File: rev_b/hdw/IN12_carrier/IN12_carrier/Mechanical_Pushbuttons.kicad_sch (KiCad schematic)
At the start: 1 part, among them U1101 MAX6818

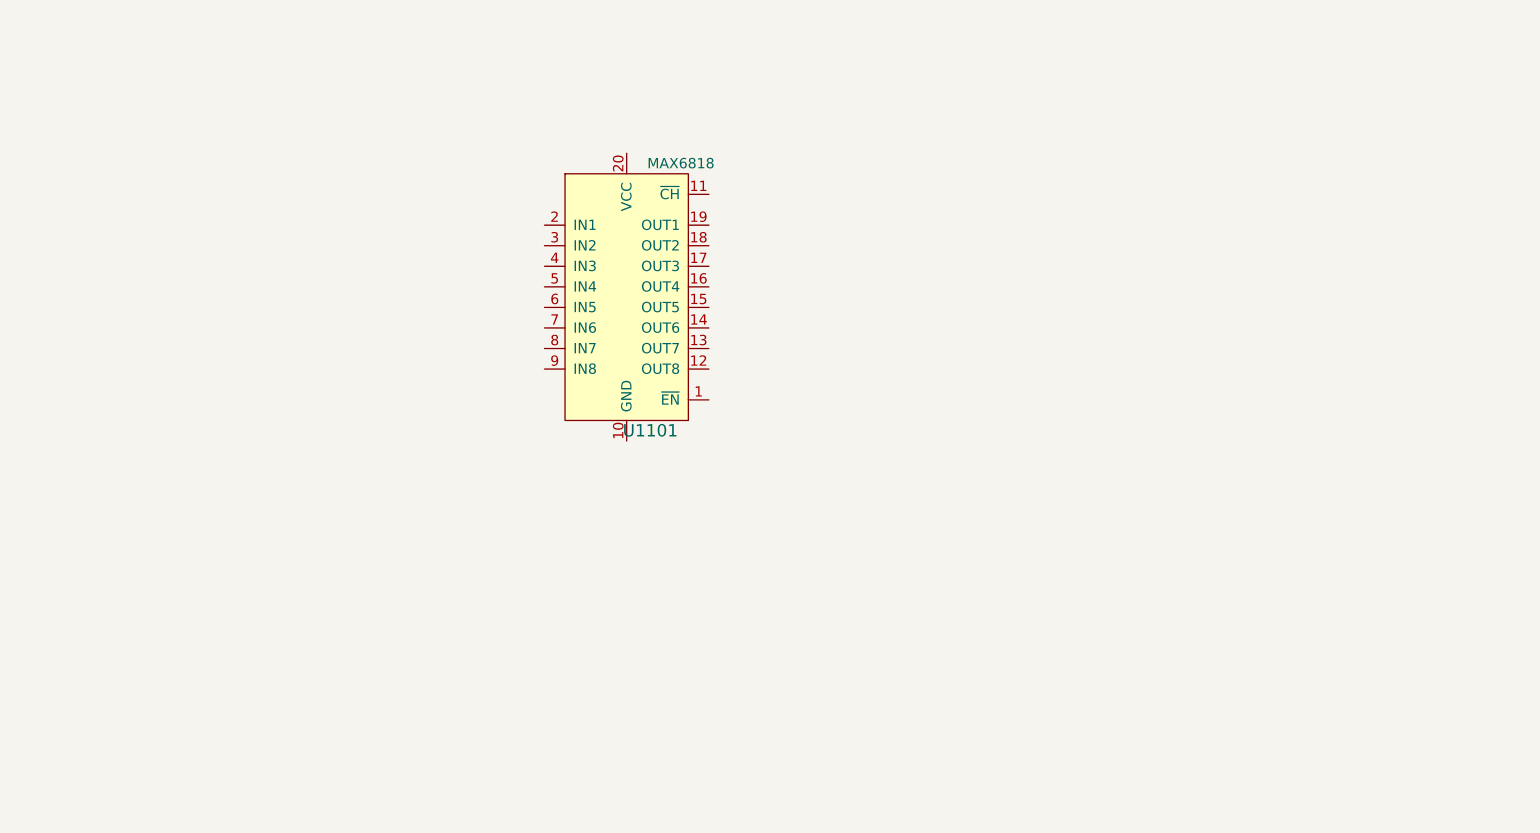
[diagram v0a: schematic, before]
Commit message: lots of placement progress on IN12 carrier board
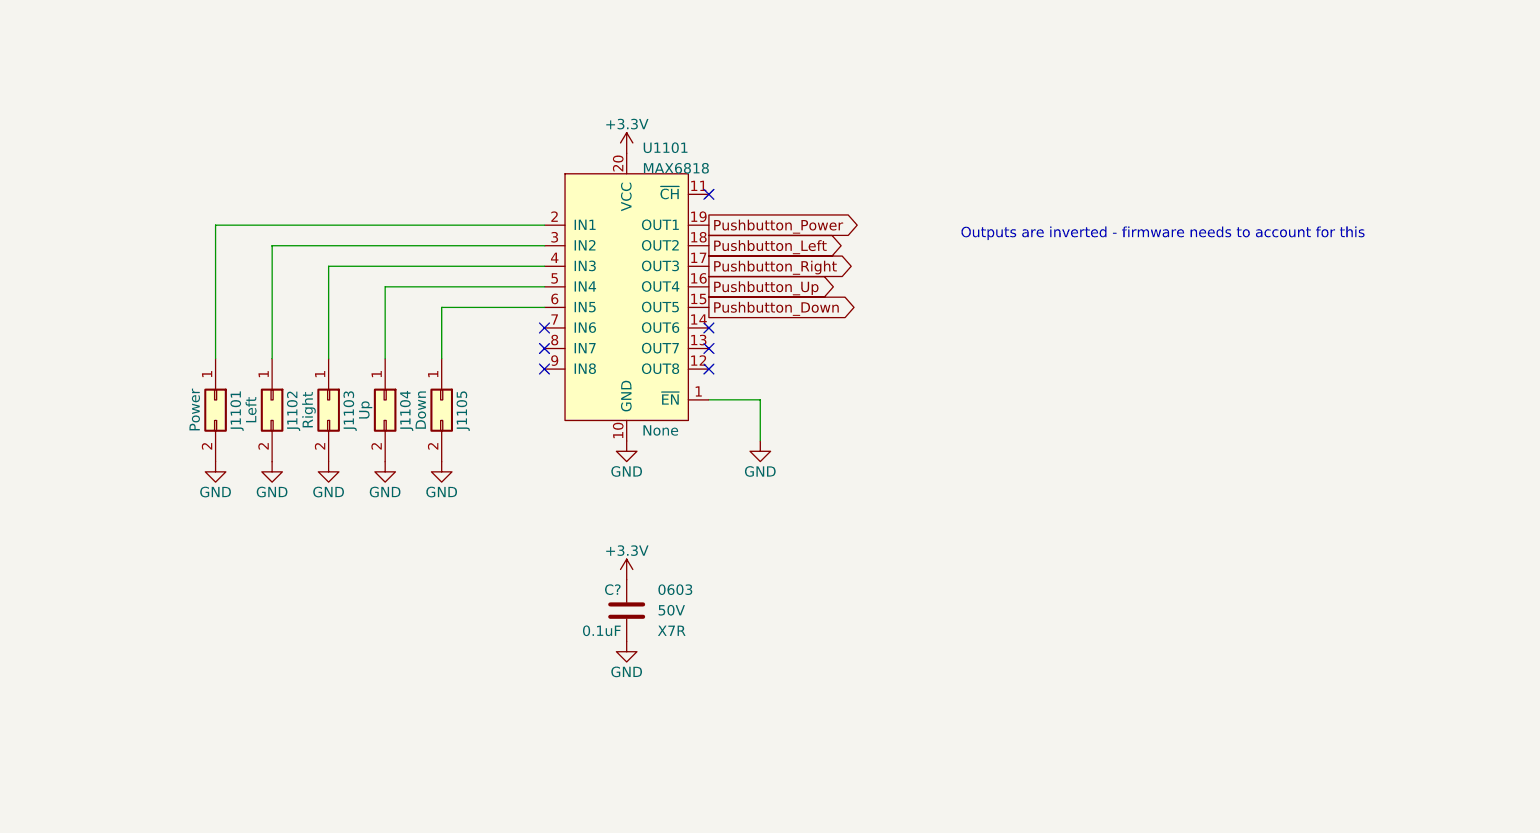
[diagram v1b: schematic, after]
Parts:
- added C?: 0.1uF, Capacitors_SMD:C_0603, symbol Custom_Library:C_Custom
- added J1101: Power, Connector_PinHeader_2.54mm:PinHeader_1x02_P2.54mm_Vertical, symbol Connector_Generic:Conn_02x01
- added J1102: Left, Connector_PinHeader_2.54mm:PinHeader_1x02_P2.54mm_Vertical, symbol Connector_Generic:Conn_02x01
- added J1103: Right, Connector_PinHeader_2.54mm:PinHeader_1x02_P2.54mm_Vertical, symbol Connector_Generic:Conn_02x01
- added J1104: Up, Connector_PinHeader_2.54mm:PinHeader_1x02_P2.54mm_Vertical, symbol Connector_Generic:Conn_02x01
- added J1105: Down, Connector_PinHeader_2.54mm:PinHeader_1x02_P2.54mm_Vertical, symbol Connector_Generic:Conn_02x01
- U1101: Configuration (none) -> None
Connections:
- net GND: now reaches U1101.1 (~{EN})
- net GND: now also U1101.10 (GND), C?.2, J1101.2 (Pin_2), J1102.2 (Pin_2), J1103.2 (Pin_2), J1104.2 (Pin_2), J1105.2 (Pin_2)
- net Pushbutton_Down: now reaches U1101.15 (OUT5)
- net Pushbutton_Up: now reaches U1101.16 (OUT4)
- net Pushbutton_Right: now reaches U1101.17 (OUT3)
- net Pushbutton_Left: now reaches U1101.18 (OUT2)
- net Pushbutton_Power: now reaches U1101.19 (OUT1)
- net at U1101.2 (IN1): now also J1101.1 (Pin_1)
- net +3.3V: now reaches U1101.20 (VCC)
- net +3.3V: now also C?.1
- net at U1101.3 (IN2): now also J1102.1 (Pin_1)
- net at U1101.4 (IN3): now also J1103.1 (Pin_1)
- net at U1101.5 (IN4): now also J1104.1 (Pin_1)
- net at U1101.6 (IN5): now also J1105.1 (Pin_1)
- no-connect marks 0 -> 7
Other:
- note added: "Outputs are inverted - firmware needs to account for this"

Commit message: lots of routing and design progress on IN12 carrier board
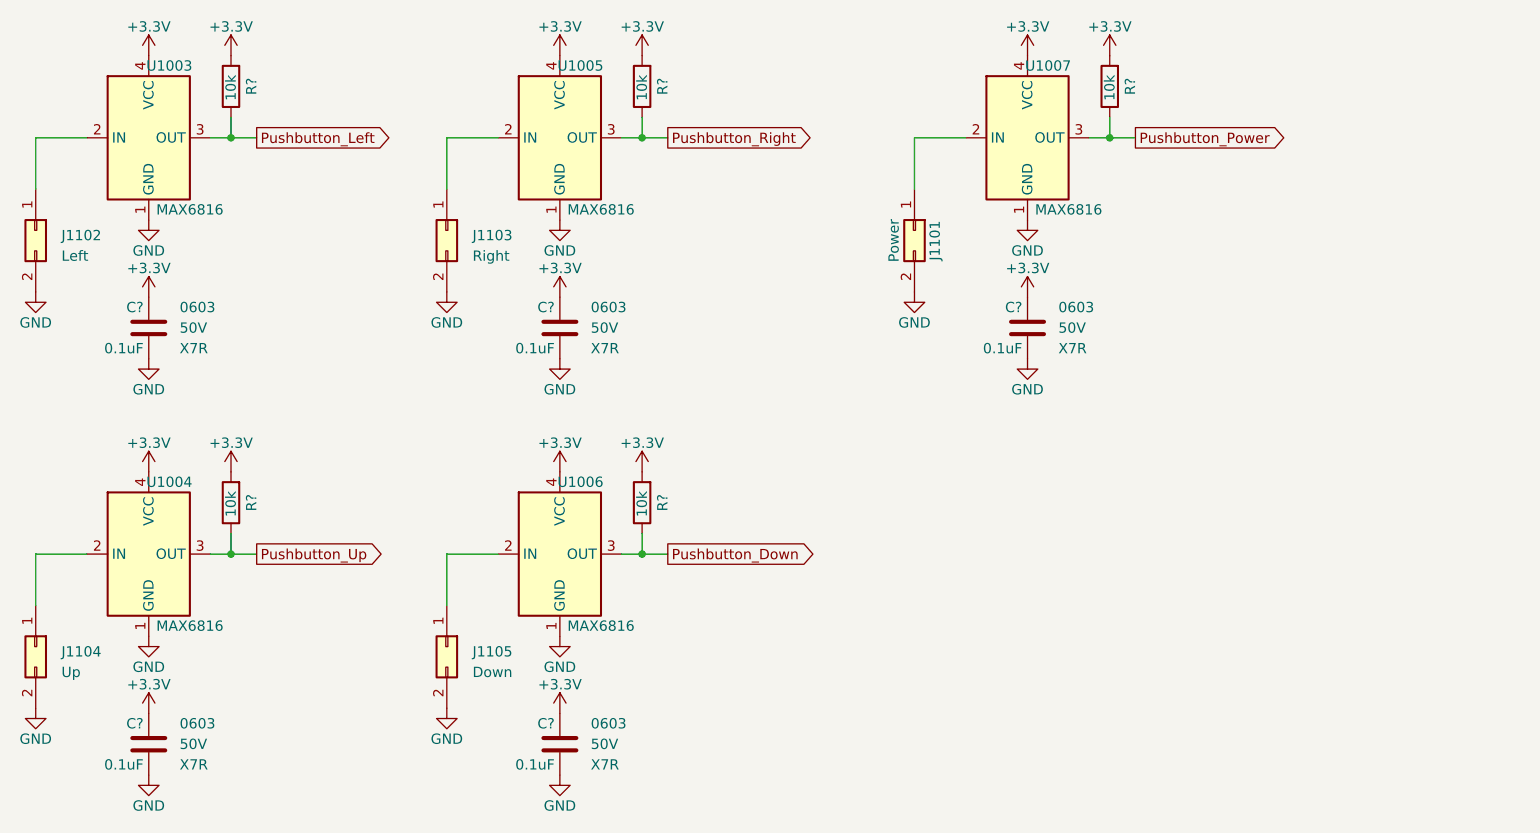
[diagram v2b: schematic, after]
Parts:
- removed C?: 0.1uF, Capacitors_SMD:C_0603, symbol Custom_Library:C_Custom
- removed U1101: MAX6818, Housings_SSOP:SSOP-20_5.3x7.2mm_Pitch0.65mm, symbol Custom Library:MAX6818
- added C? (x5): 0.1uF, Capacitors_SMD:C_0603, symbol Custom_Library:C_Custom
- added R? (x5): 10k, Resistors_SMD:R_0603, symbol Custom_Library:R_Custom
- added U1003, U1004, U1005, U1006, U1007: MAX6816, Package_TO_SOT_SMD:SOT-143, symbol Interface:MAX6816
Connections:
- net +3.3V: now also C?.1, C?.1, C?.1, C?.1, C?.1, R?.1, R?.1, R?.1, R?.1, R?.1, U1003.4 (VCC), U1004.4 (VCC), U1005.4 (VCC), U1006.4 (VCC), U1007.4 (VCC)
- net GND: now also C?.2, C?.2, C?.2, C?.2, C?.2, U1003.1 (GND), U1004.1 (GND), U1005.1 (GND), U1006.1 (GND), U1007.1 (GND)
- net Pushbutton_Down: now also R?.2, U1006.3 (OUT)
- net Pushbutton_Left: now also R?.2, U1003.3 (OUT)
- net Pushbutton_Power: now also R?.2, U1007.3 (OUT)
- net Pushbutton_Right: now also R?.2, U1005.3 (OUT)
- net Pushbutton_Up: now also R?.2, U1004.3 (OUT)
- net at J1103.1 (Pin_1): now also U1005.2 (IN)
- net at J1101.1 (Pin_1): now also U1007.2 (IN)
- net at J1102.1 (Pin_1): now also U1003.2 (IN)
- net at J1105.1 (Pin_1): now also U1006.2 (IN)
- net at J1104.1 (Pin_1): now also U1004.2 (IN)
- no-connect marks 7 -> 0
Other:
- note removed: "Outputs are inverted - firmware needs to account for this"
- moved on the sheet: J1101, J1102, J1103, J1104, J1105
